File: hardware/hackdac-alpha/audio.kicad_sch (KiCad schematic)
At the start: 26 parts, among them J4 I2C, J5 AUDIO OUT, P2 P22, U10 PCM5102, U8 MCP1700T-3302E/MB, U9 TCA9517D

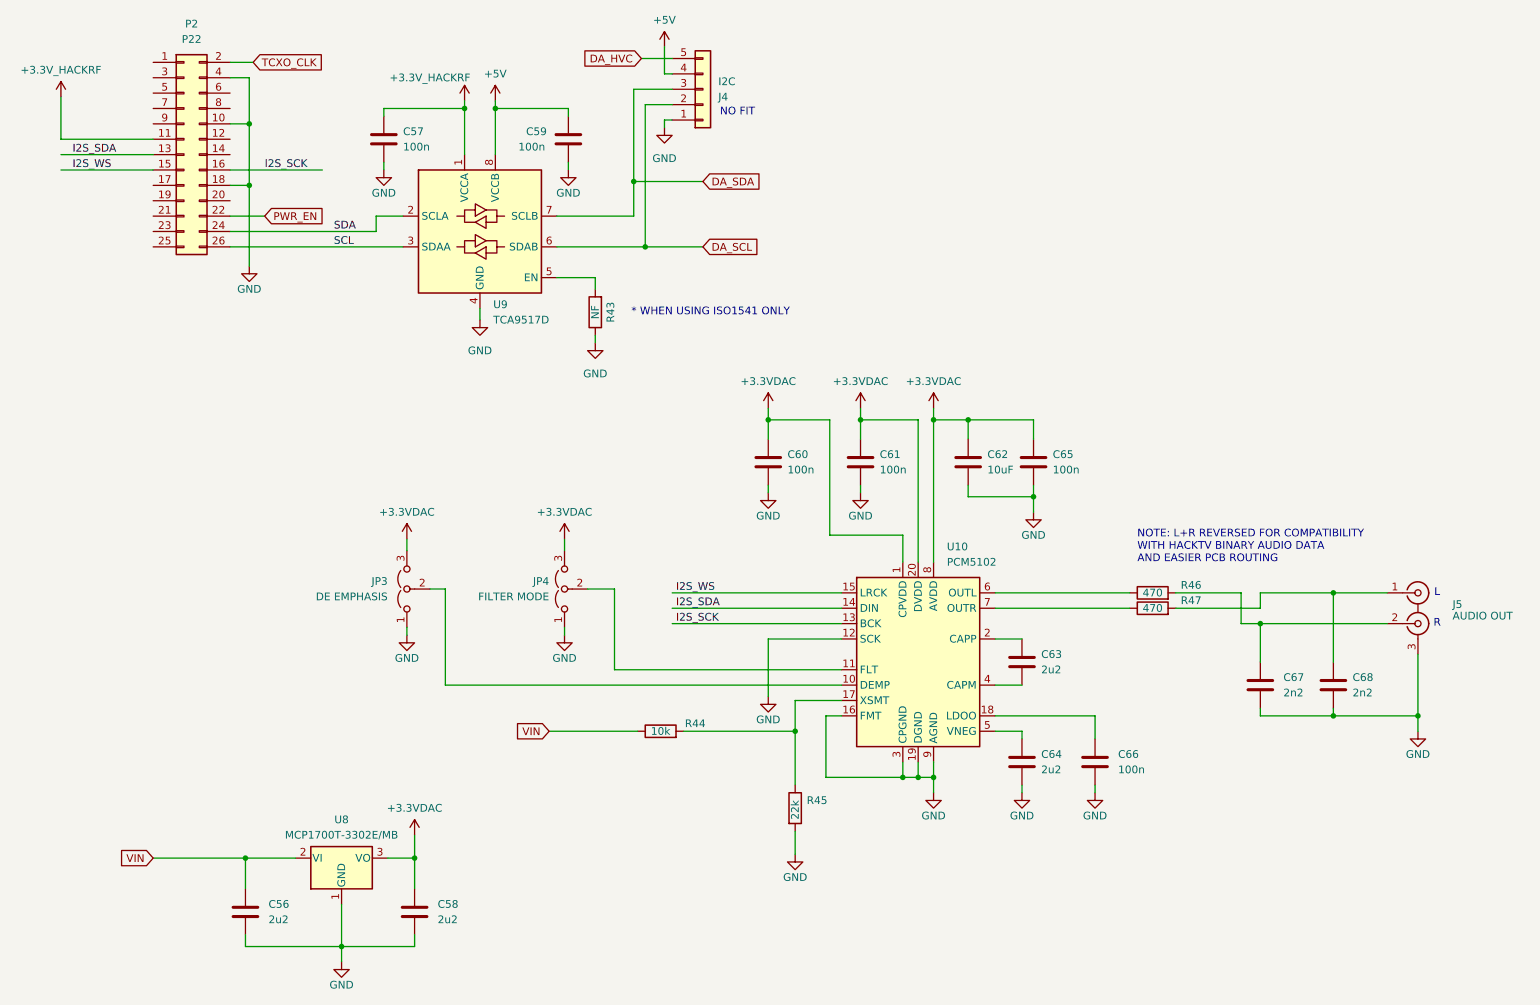
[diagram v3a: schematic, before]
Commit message: Added configuration straps
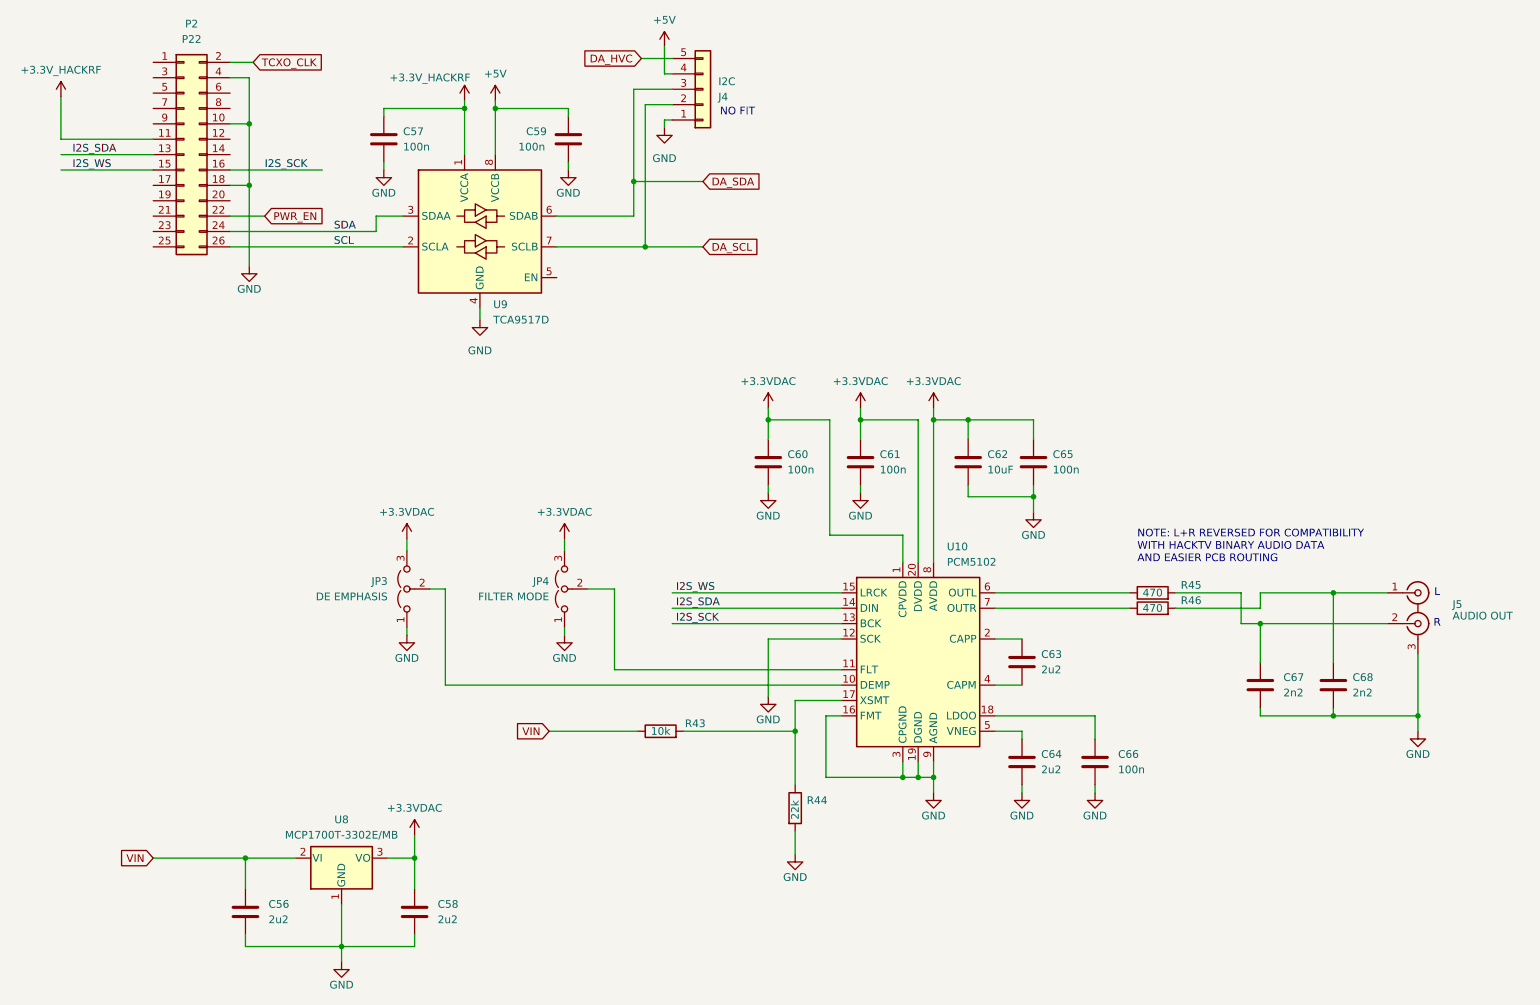
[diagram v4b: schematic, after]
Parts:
- removed R43: NF, Resistor_SMD:R_0603_1608Metric, symbol Device:R
- renumbered R44 to R43, R45 to R44, R46 to R45, R47 to R46
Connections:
- net DA_SCL: now also U9.7 (SCLB); no longer U9.6 (SDAB)
- net DA_SDA: now also U9.6 (SDAB); no longer U9.7 (SCLB)
- net SCL: now also U9.2 (SCLA); no longer U9.3 (SDAA)
- net SDA: now also U9.3 (SDAA); no longer U9.2 (SCLA)
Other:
- note removed: "* WHEN USING ISO1541 ONLY"
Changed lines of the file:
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@@
 	(wire
 		(pts
-			(xy 114.935 62.865) (xy 114.935 64.77)
-		)
-		(stroke
-			(width 0)
-			(type default)
-		)
-	)
-	(wire
-		(pts
 			(xy 57.785 47.625) (xy 57.785 60.96)
 		)
@@
 	(wire
 		(pts
-			(xy 108.585 62.865) (xy 114.935 62.865)
-		)
-		(stroke
-			(width 0)
-			(type default)
-		)
-	)
-	(wire
-		(pts
 			(xy 98.425 34.925) (xy 98.425 42.545)
 		)
@@
 	(wire
 		(pts
-			(xy 114.935 72.39) (xy 114.935 73.66)
-		)
-		(stroke
-			(width 0)
-			(type default)
-		)
-	)
-	(wire
-		(pts
 			(xy 153.67 86.36) (xy 153.67 105.41)
 		)
@@
 		)
 	)
-	(text "* WHEN USING ISO1541 ONLY"
-		(exclude_from_sim no)
-		(at 133.985 68.58 0)
-		(effects
-			(font
-				(size 1.27 1.27)
-			)
-		)
-	)
 	(text "NOTE: L+R REVERSED FOR COMPATIBILITY\nWITH HACKTV BINARY AUDIO DATA\nAND EASIER PCB ROUTING"
 		(exclude_from_sim no)
@@
 		(dnp no)
 		(fields_autoplaced yes)
-		(property "Reference" "#PWR0102"
+		(property "Reference" "#PWR0101"
 			(at 174.625 85.725 0)
 			(effects
@@
 			(project "dacattac-alpha"
 				(path "/487245ca-0c1f-4f9d-bc99-20c8f558090f/80e17ed4-cb43-4c12-a09c-75e0f0ffaba0"
-					(reference "#PWR0102")
-					(unit 1)
-				)
-			)
-		)
-	)
-	(symbol
-		(lib_name "GND_2")
-		(lib_id "power:GND")
-		(at 114.935 73.66 0)
-		(unit 1)
-		(exclude_from_sim no)
-		(in_bom yes)
-		(on_board yes)
-		(dnp no)
-		(fields_autoplaced yes)
-		(property "Reference" "#PWR093"
-			(at 114.935 80.01 0)
-			(effects
-				(font
-					(size 1.27 1.27)
-				)
-				(hide yes)
-			)
-		)
-		(property "Value" "GND"
-			(at 114.935 78.74 0)
-			(effects
-				(font
-					(size 1.27 1.27)
-				)
-			)
-		)
-		(property "Footprint" ""
-			(at 114.935 73.66 0)
-			(effects
-				(font
-					(size 1.27 1.27)
-				)
-				(hide yes)
-			)
-		)
-		(property "Datasheet" ""
-			(at 114.935 73.66 0)
-			(effects
-				(font
-					(size 1.27 1.27)
-				)
-				(hide yes)
-			)
-		)
-		(property "Description" "Power symbol creates a global label with name \"GND\" , ground"
-			(at 114.935 73.66 0)
-			(effects
-				(font
-					(size 1.27 1.27)
-				)
-				(hide yes)
-			)
-		)
-		(pin "1"
-		)
-		(instances
-			(project ""
-				(path "/487245ca-0c1f-4f9d-bc99-20c8f558090f/80e17ed4-cb43-4c12-a09c-75e0f0ffaba0"
-					(reference "#PWR093")
+					(reference "#PWR0101")
 					(unit 1)
 				)
@@
 		(on_board yes)
 		(dnp no)
-		(property "Reference" "R47"
+		(property "Reference" "R46"
 			(at 213.36 116.205 90)
 			(effects
@@
 			(project "dacattac-alpha"
 				(path "/487245ca-0c1f-4f9d-bc99-20c8f558090f/80e17ed4-cb43-4c12-a09c-75e0f0ffaba0"
-					(reference "R47")
+					(reference "R46")
 					(unit 1)
 				)
@@
 		(on_board yes)
 		(dnp no)
-		(property "Reference" "#PWR0105"
+		(property "Reference" "#PWR0104"
 			(at 187.325 107.95 0)
 			(effects
@@
 			(project "dacattac-alpha"
 				(path "/487245ca-0c1f-4f9d-bc99-20c8f558090f/80e17ed4-cb43-4c12-a09c-75e0f0ffaba0"
-					(reference "#PWR0105")
+					(reference "#PWR0104")
 					(unit 1)
 				)
@@
 		(on_board yes)
 		(dnp no)
-		(property "Reference" "#PWR097"
+		(property "Reference" "#PWR096"
 			(at 143.51 104.775 0)
 			(effects
@@
 			(project "dacattac-alpha"
 				(path "/487245ca-0c1f-4f9d-bc99-20c8f558090f/80e17ed4-cb43-4c12-a09c-75e0f0ffaba0"
-					(reference "#PWR097")
+					(reference "#PWR096")
 					(unit 1)
 				)
@@
 		(on_board yes)
 		(dnp no)
-		(property "Reference" "#PWR0106"
+		(property "Reference" "#PWR0105"
 			(at 197.485 154.305 0)
 			(effects
@@
 			(project "dacattac-alpha"
 				(path "/487245ca-0c1f-4f9d-bc99-20c8f558090f/80e17ed4-cb43-4c12-a09c-75e0f0ffaba0"
-					(reference "#PWR0106")
+					(reference "#PWR0105")
 					(unit 1)
 				)
@@
 		(on_board yes)
 		(dnp no)
-		(property "Reference" "#PWR0103"
+		(property "Reference" "#PWR0102"
 			(at 170.815 154.305 0)
 			(effects
@@
 			(project "dacattac-alpha"
 				(path "/487245ca-0c1f-4f9d-bc99-20c8f558090f/80e17ed4-cb43-4c12-a09c-75e0f0ffaba0"
-					(reference "#PWR0103")
+					(reference "#PWR0102")
 					(unit 1)
 				)
@@
 		(on_board yes)
 		(dnp no)
-		(property "Reference" "R46"
+		(property "Reference" "R45"
 			(at 213.36 113.665 90)
 			(effects
@@
 			(project "dacattac-alpha"
 				(path "/487245ca-0c1f-4f9d-bc99-20c8f558090f/80e17ed4-cb43-4c12-a09c-75e0f0ffaba0"
-					(reference "R46")
+					(reference "R45")
 					(unit 1)
 				)
@@
 		(on_board yes)
 		(dnp no)
-		(property "Reference" "R44"
+		(property "Reference" "R43"
 			(at 131.445 136.525 90)
 			(effects
@@
 			(project "dacattac-alpha"
 				(path "/487245ca-0c1f-4f9d-bc99-20c8f558090f/80e17ed4-cb43-4c12-a09c-75e0f0ffaba0"
-					(reference "R44")
+					(reference "R43")
 					(unit 1)
 				)
@@
 	)
 	(symbol
-		(lib_id "Device:R")
-		(at 114.935 68.58 180)
-		(unit 1)
-		(exclude_from_sim no)
-		(in_bom yes)
-		(on_board yes)
-		(dnp no)
-		(property "Reference" "R43"
-			(at 117.475 68.58 90)
-			(effects
-				(font
-					(size 1.27 1.27)
-				)
-			)
-		)
-		(property "Value" "NF"
-			(at 114.935 68.58 90)
-			(effects
-				(font
-					(size 1.27 1.27)
-				)
-			)
-		)
-		(property "Footprint" "Resistor_SMD:R_0603_1608Metric"
-			(at 116.713 68.58 90)
-			(effects
-				(font
-					(size 1.27 1.27)
-				)
-				(hide yes)
-			)
-		)
-		(property "Datasheet" "~"
-			(at 114.935 68.58 0)
-			(effects
-				(font
-					(size 1.27 1.27)
-				)
-				(hide yes)
-			)
-		)
-		(property "Description" ""
-			(at 114.935 68.58 0)
-			(effects
-				(font
-					(size 1.27 1.27)
-				)
-				(hide yes)
-			)
-		)
-		(pin "2"
-		)
-		(pin "1"
-		)
-		(instances
-			(project "hackdac-alpha"
-				(path "/487245ca-0c1f-4f9d-bc99-20c8f558090f/80e17ed4-cb43-4c12-a09c-75e0f0ffaba0"
-					(reference "R43")
-					(unit 1)
-				)
-			)
-		)
-	)
-	(symbol
 		(lib_id "Device:C")
 		(at 85.09 167.64 0)
@@
 		(on_board yes)
 		(dnp no)
-		(property "Reference" "#PWR094"
+		(property "Reference" "#PWR093"
 			(at 126.365 28.575 0)
 			(effects
@@
 			(project "dacattac-alpha"
 				(path "/487245ca-0c1f-4f9d-bc99-20c8f558090f/80e17ed4-cb43-4c12-a09c-75e0f0ffaba0"
-					(reference "#PWR094")
+					(reference "#PWR093")
 					(unit 1)
 				)
@@
 		(on_board yes)
 		(dnp no)
-		(property "Reference" "#PWR098"
+		(property "Reference" "#PWR097"
 			(at 143.51 138.43 0)
 			(effects
@@
 			(project "dacattac-alpha"
 				(path "/487245ca-0c1f-4f9d-bc99-20c8f558090f/80e17ed4-cb43-4c12-a09c-75e0f0ffaba0"
-					(reference "#PWR098")
+					(reference "#PWR097")
 					(unit 1)
 				)
@@
 		(dnp no)
 		(fields_autoplaced yes)
-		(property "Reference" "#PWR096"
+		(property "Reference" "#PWR095"
 			(at 147.32 85.725 0)
 			(effects
@@
 			(project "dacattac-alpha"
 				(path "/487245ca-0c1f-4f9d-bc99-20c8f558090f/80e17ed4-cb43-4c12-a09c-75e0f0ffaba0"
-					(reference "#PWR096")
+					(reference "#PWR095")
 					(unit 1)
 				)
@@
 		(on_board yes)
 		(dnp no)
-		(property "Reference" "#PWR099"
+		(property "Reference" "#PWR098"
 			(at 147.955 164.465 0)
 			(effects
@@
 			(project "dacattac-alpha"
 				(path "/487245ca-0c1f-4f9d-bc99-20c8f558090f/80e17ed4-cb43-4c12-a09c-75e0f0ffaba0"
-					(reference "#PWR099")
+					(reference "#PWR098")
 					(unit 1)
 				)
@@
 		(on_board yes)
 		(dnp no)
-		(property "Reference" "#PWR0104"
+		(property "Reference" "#PWR0103"
 			(at 185.42 154.305 0)
 			(effects
@@
 			(project "dacattac-alpha"
 				(path "/487245ca-0c1f-4f9d-bc99-20c8f558090f/80e17ed4-cb43-4c12-a09c-75e0f0ffaba0"
-					(reference "#PWR0104")
+					(reference "#PWR0103")
 					(unit 1)
 				)
@@
 		(dnp no)
 		(fields_autoplaced yes)
-		(property "Reference" "#PWR095"
+		(property "Reference" "#PWR094"
 			(at 126.365 44.45 0)
 			(effects
@@
 			(project "dacattac-alpha"
 				(path "/487245ca-0c1f-4f9d-bc99-20c8f558090f/80e17ed4-cb43-4c12-a09c-75e0f0ffaba0"
-					(reference "#PWR095")
+					(reference "#PWR094")
 					(unit 1)
 				)
@@
 		(on_board yes)
 		(dnp no)
-		(property "Reference" "R45"
+		(property "Reference" "R44"
 			(at 149.86 149.225 0)
 			(effects
@@
 			(project "dacattac-alpha"
 				(path "/487245ca-0c1f-4f9d-bc99-20c8f558090f/80e17ed4-cb43-4c12-a09c-75e0f0ffaba0"
-					(reference "R45")
+					(reference "R44")
 					(unit 1)
 				)
@@
 		(on_board yes)
 		(dnp no)
-		(property "Reference" "#PWR0107"
+		(property "Reference" "#PWR0106"
 			(at 250.825 144.145 0)
 			(effects
@@
 			(project "dacattac-alpha"
 				(path "/487245ca-0c1f-4f9d-bc99-20c8f558090f/80e17ed4-cb43-4c12-a09c-75e0f0ffaba0"
-					(reference "#PWR0107")
+					(reference "#PWR0106")
 					(unit 1)
 				)
@@
 		(on_board yes)
 		(dnp no)
-		(property "Reference" "#PWR0101"
+		(property "Reference" "#PWR0100"
 			(at 158.75 104.775 0)
 			(effects
@@
 			(project "dacattac-alpha"
 				(path "/487245ca-0c1f-4f9d-bc99-20c8f558090f/80e17ed4-cb43-4c12-a09c-75e0f0ffaba0"
-					(reference "#PWR0101")
+					(reference "#PWR0100")
 					(unit 1)
 				)
@@
 		(dnp no)
 		(fields_autoplaced yes)
-		(property "Reference" "#PWR0100"
+		(property "Reference" "#PWR099"
 			(at 162.56 85.725 0)
 			(effects
@@
 			(project "dacattac-alpha"
 				(path "/487245ca-0c1f-4f9d-bc99-20c8f558090f/80e17ed4-cb43-4c12-a09c-75e0f0ffaba0"
-					(reference "#PWR0100")
+					(reference "#PWR099")
 					(unit 1)
 				)

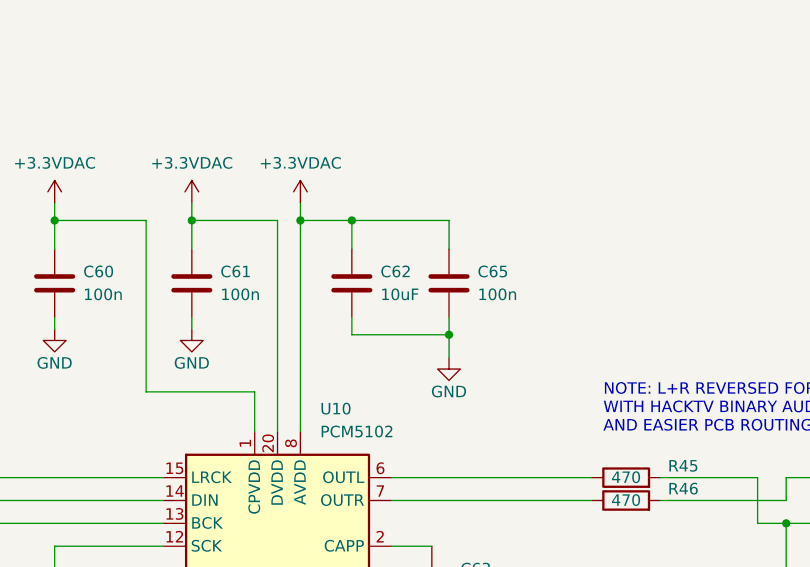
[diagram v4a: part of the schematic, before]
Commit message: Fixed a couple of incorrect component values
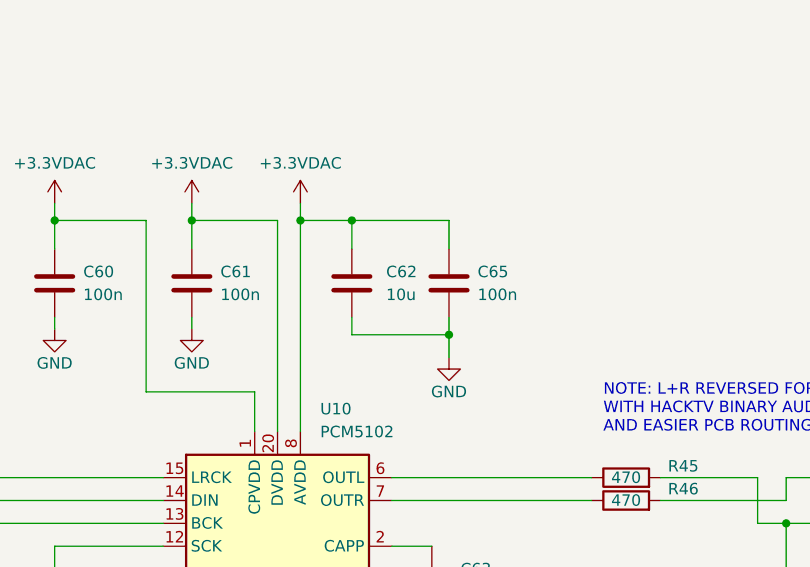
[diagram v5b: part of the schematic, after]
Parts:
- C62: value 10uF -> 10u
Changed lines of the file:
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@@
 		(fields_autoplaced yes)
 		(property "Reference" "C62"
-			(at 179.705 92.075 0)
+			(at 180.34 92.0749 0)
 			(effects
 				(font
@@
 			)
 		)
-		(property "Value" "10uF"
-			(at 179.705 94.615 0)
+		(property "Value" "10u"
+			(at 180.34 94.6149 0)
 			(effects
 				(font

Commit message: Fixed a couple of incorrect component values
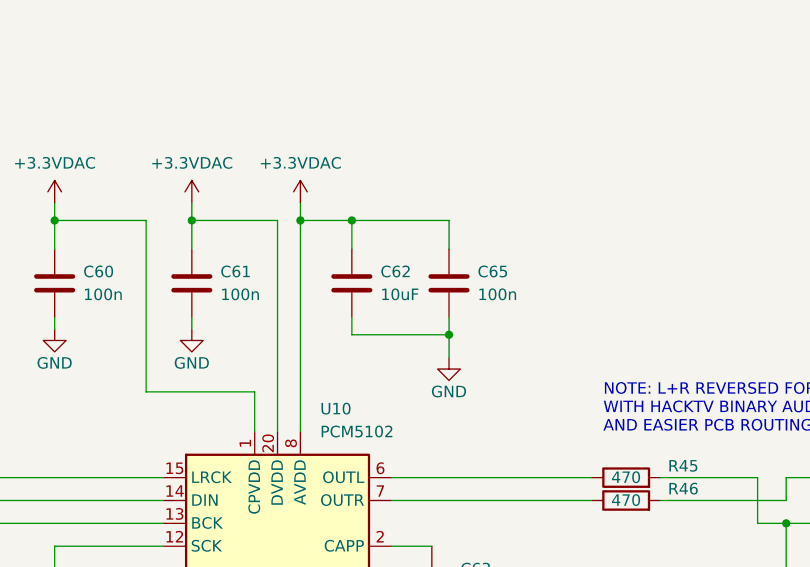
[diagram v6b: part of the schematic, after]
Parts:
- C62: value 10u -> 10uF
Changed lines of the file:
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@@
 		(fields_autoplaced yes)
 		(property "Reference" "C62"
-			(at 180.34 92.0749 0)
+			(at 179.705 92.075 0)
 			(effects
 				(font
@@
 			)
 		)
-		(property "Value" "10u"
-			(at 180.34 94.6149 0)
+		(property "Value" "10uF"
+			(at 179.705 94.615 0)
 			(effects
 				(font
